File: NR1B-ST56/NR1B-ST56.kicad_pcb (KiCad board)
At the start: 4 copper layers, 70.5 x 134 mm, 44 parts, among them J1 0.1" Female Long Tail, J2 0.1" Female Long Tail, J3 Conn_01x02, U1 S29GL01GP, U2 DG419LDY, U3 OPA2189ID, U4 NCV7800, X1 NUCLEO144-ZIO

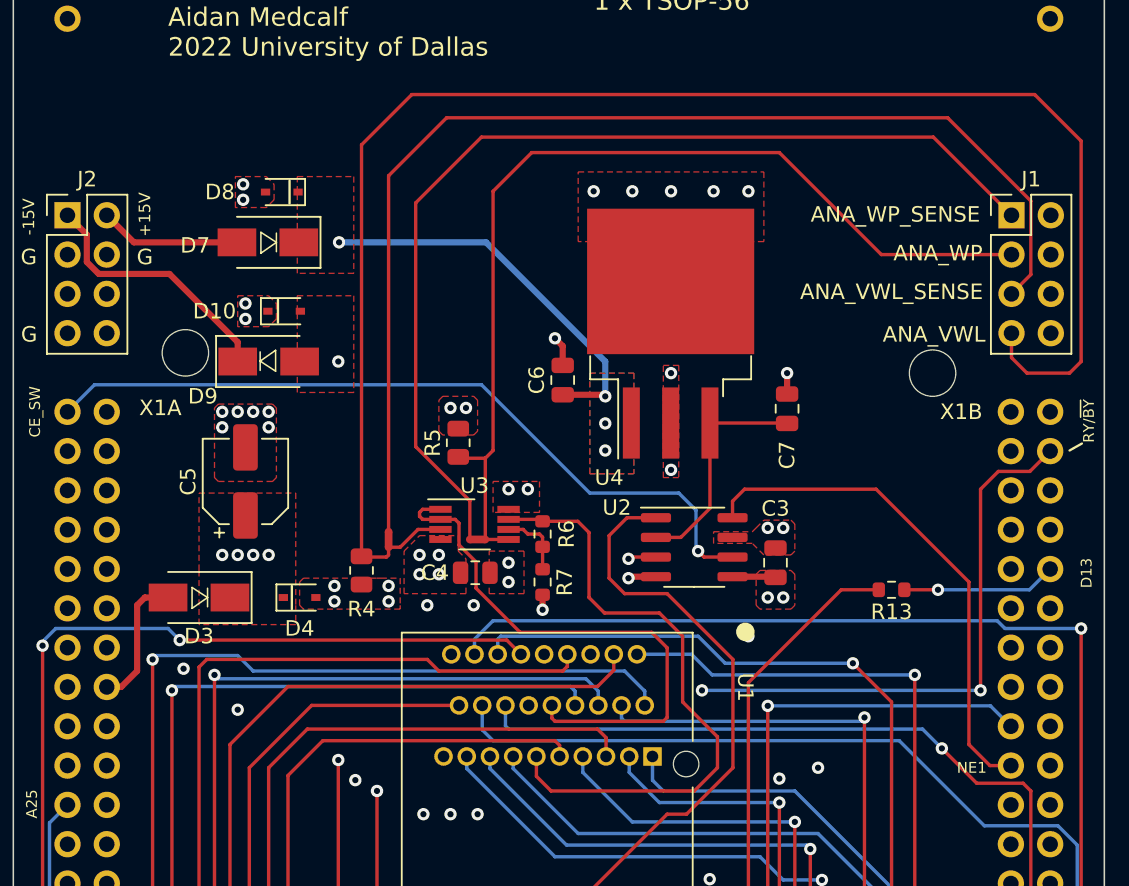
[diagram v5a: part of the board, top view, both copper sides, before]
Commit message: Replaced dual op amp with two single op amps
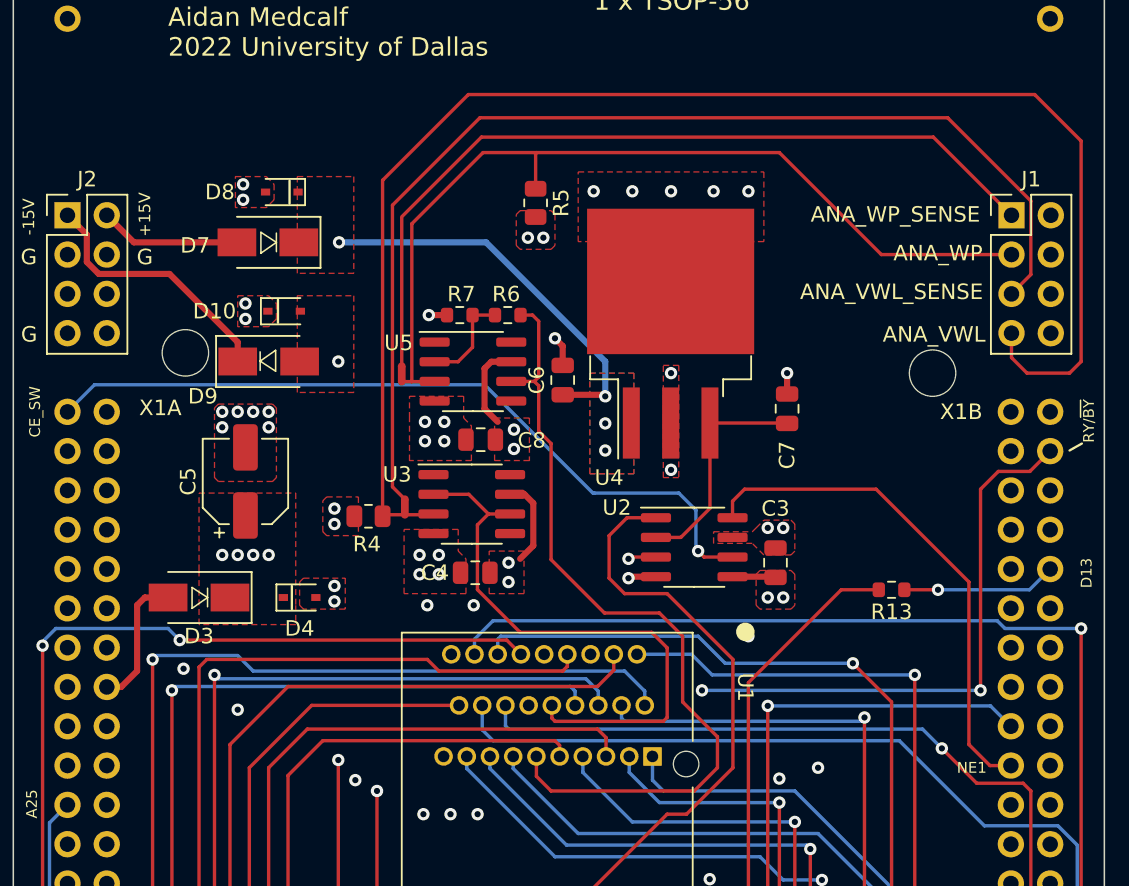
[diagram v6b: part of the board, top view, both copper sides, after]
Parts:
- added C8: 0.1uF, Capacitor_SMD:C_0805_2012Metric, F.Cu at (195.2, 112.8)
- added U5: OPA189ID, Package_SO:SOIC-8_3.9x4.9mm_P1.27mm, F.Cu at (194.7, 108.4)
- U3: value OPA2189ID -> OPA189ID; footprint Package_SO:VSSOP-8_3.0x3.0mm_P0.65mm -> Package_SO:SOIC-8_3.9x4.9mm_P1.27mm
- U4: value NCV7800 -> NCV7809
- moved R7 18.1 mm to (193.8, 104.8), turned to 180 degrees
- moved R5 16.3 mm to (198.8, 97.5), turned to -90 degrees
- moved R6 14.3 mm to (196.9, 104.8), turned to 0 degrees
- moved NT2 11.8 mm to (190.1, 108.5), turned to 90 degrees
- moved R4 3.53 mm to (187.9, 117.8), turned to 180 degrees
- moved NT1 2.35 mm to (190.3, 117.2)
- moved U3 1.32 mm to (194.6, 117.0)
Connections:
- U3 pad 1: /VWL_BUF -> unconnected-(U3-Pad1)
- U3 pad 5: /ANA_WP -> unconnected-(U3-Pad5)
- U3 pad 6: Net-(R6-Pad1) -> /VWL_BUF
- U3 pad 7: /WP_BUF -> +15V
- U3 pad 8: +15V -> unconnected-(U3-Pad8)
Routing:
- net /WP_BUF: track 40.3 -> 52.8 mm
- net /ANA_WP_SENSE: track 65.6 -> 53.2 mm
- net +15V: track 27.2 -> 38.6 mm
- net /ANA_VWL: track 102.9 -> 94.8 mm
- net /ANA_WP: track 63.3 -> 58.1 mm
- net /ANA_VWL_SENSE: track 74.8 -> 71.7 mm
- net Net-(R6-Pad1): track 4.48 -> 6.36 mm
- net -15V: track 15.3 -> 17.1 mm, vias 5 -> 9
- net /VWL_BUF: track 36.0 -> 37.4 mm
